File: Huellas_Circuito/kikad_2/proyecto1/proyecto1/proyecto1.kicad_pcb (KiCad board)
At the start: 2 copper layers, 54.5 x 77.5 mm, 6 parts, among them U1 ESP32-DEVKIT-V1

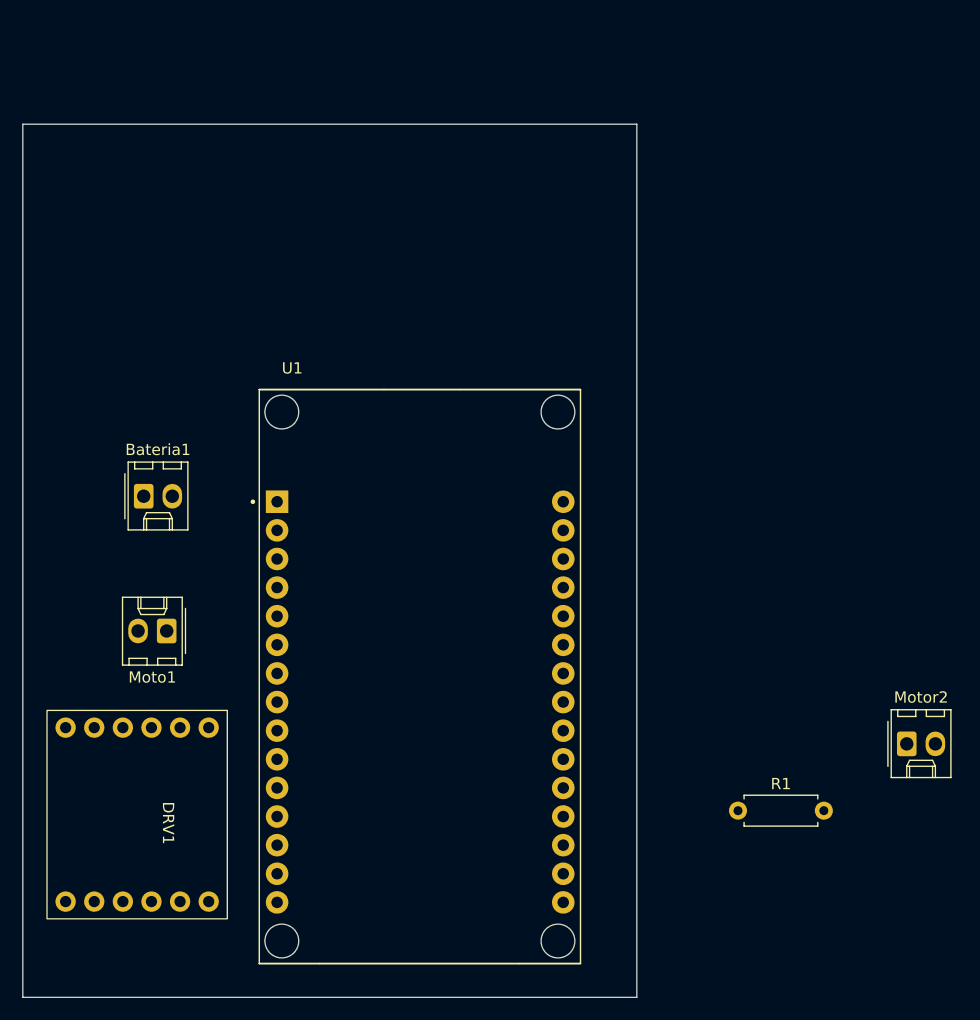
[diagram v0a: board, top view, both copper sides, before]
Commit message: Creacion_Footprint_Regul&Conectado
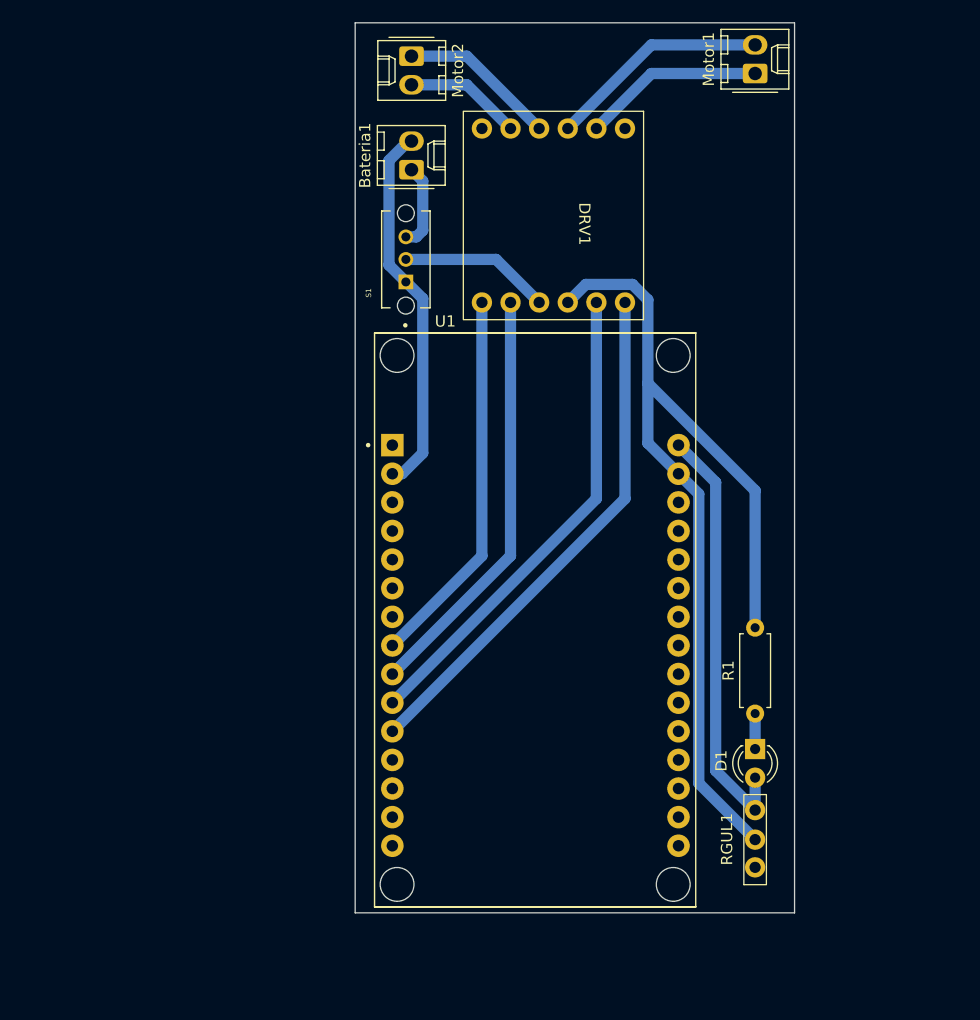
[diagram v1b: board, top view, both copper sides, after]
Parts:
- removed Moto1: Screw_Terminal_01x02, Connector_Molex:Molex_KK-254_AE-6410-02A_1x02_P2.54mm_Vertical
- added D1: LED, LED_THT:LED_D3.0mm, F.Cu at (145.5, 96.5)
- added Motor1: Screw_Terminal_01x02, Connector_Molex:Molex_KK-254_AE-6410-02A_1x02_P2.54mm_Vertical, F.Cu at (145.5, 36.5)
- added RGUL1: ~, Regulador:RGUL1, F.Cu at (145.5, 104.5)
- added S1: OS102011MS2QN1, OS102011MS2QN1:SW_OS102011MS2QN1, F.Cu at (114.5, 53.0)
- moved Motor2 75.2 mm to (115.0, 35.0), turned to -90 degrees
- moved DRV1 64.8 mm to (119.6, 39.9)
- moved Bateria1 37.5 mm to (115.0, 45.0), turned to 90 degrees
- moved U1 11.4 mm to (126.0, 85.0)
- moved R1 8.75 mm to (145.5, 93.3), turned to 90 degrees
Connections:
- U1 pad 30: /VIN -> /Vin
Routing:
- net GND: track 0.00 -> 119.3 mm
- net /PWM_MDER2: track 0.00 -> 46.6 mm
- net /PWM_MDER1: track 0.00 -> 43.0 mm
- net /Vin: track 0.00 -> 38.2 mm
- net /PWM_MIZQ2: track 0.00 -> 37.3 mm
- net /PWM_MIZQ1: track 0.00 -> 33.7 mm
- net /MIZQ2: track 0.00 -> 19.7 mm
- net /MIZQ1: track 0.00 -> 16.1 mm
- net /MDER1: track 0.00 -> 14.0 mm
- net /VDRV: track 0.00 -> 13.4 mm
- net /MDER2: track 0.00 -> 10.4 mm
- net Net-(Bateria1-Pin_1): track 0.00 -> 7.54 mm
- net Net-(D1-K): track 0.00 -> 3.15 mm
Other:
- board size 54.5 x 77.5 mm -> 39 x 79 mm

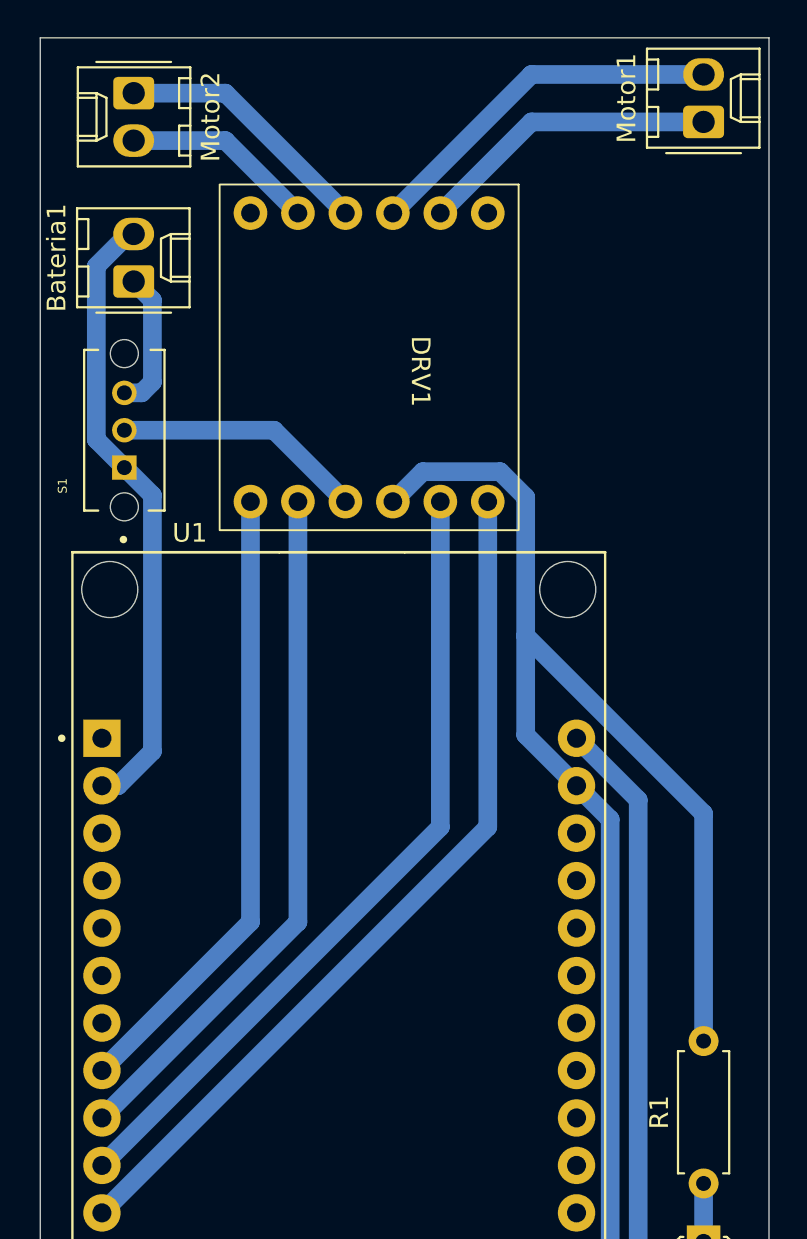
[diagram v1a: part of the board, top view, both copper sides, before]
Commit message: Actualizacion Huellas DRV (NotDefinitive)
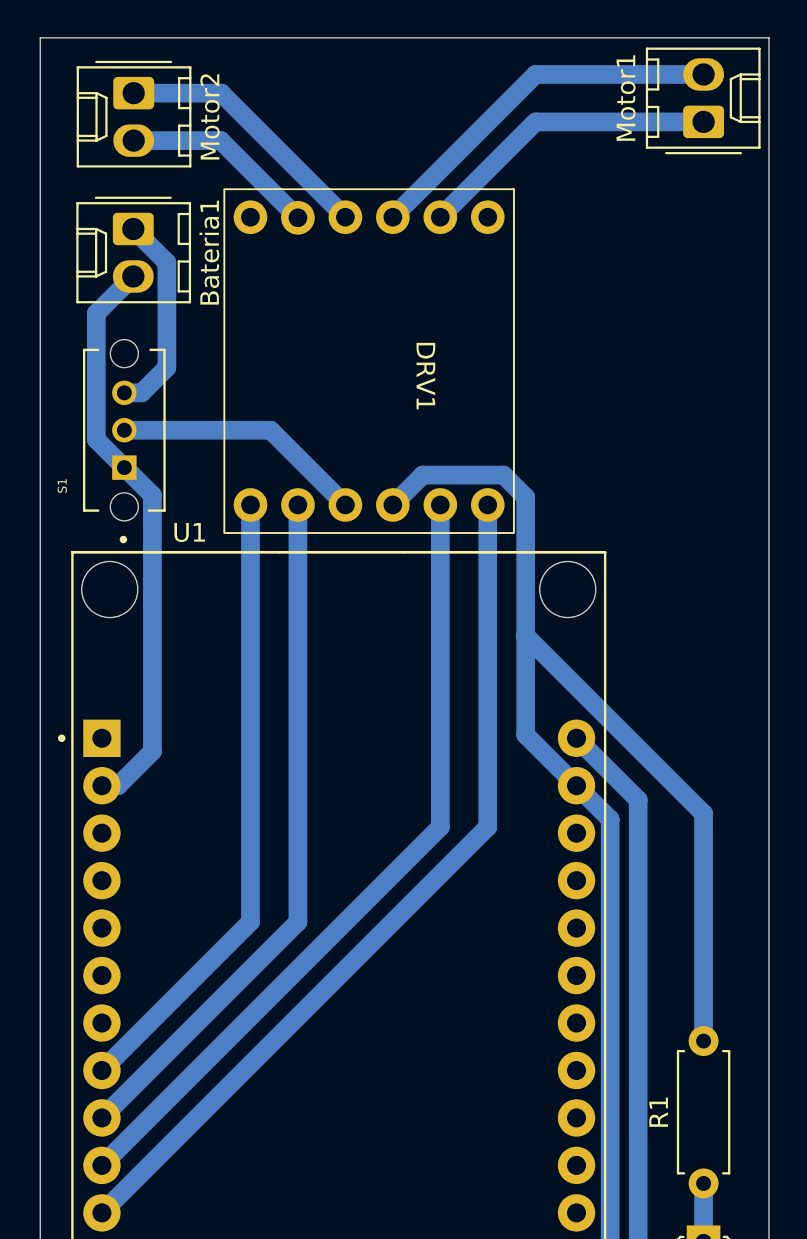
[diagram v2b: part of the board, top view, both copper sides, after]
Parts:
- moved Bateria1 2.81 mm to (115.0, 42.2), turned to -90 degrees
- moved DRV1 0.35 mm to (119.8, 40.1)
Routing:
- net Net-(Bateria1-Pin_1): track 7.54 -> 11.3 mm
- net GND: track 119.3 -> 116.7 mm

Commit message: Actualizacion Huellas DRV (NotDefinitive) V2
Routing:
- net /VDRV: track 13.5 -> 85.3 mm
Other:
- board size 39 x 79 mm -> 40 x 79 mm
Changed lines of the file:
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@@
 	(gr_rect
 		(start 110 32)
-		(end 149 111)
+		(end 150 111)
 		(stroke
 			(width 0.05)
@@
 		(end 122.33 53)
 		(width 1)
+		(layer "B.Cu")
+		(net 25)
+	)
+	(segment
+		(start 145.5 106.96)
+		(end 147.101 105.359)
+		(width 1)
+		(layer "B.Cu")
+		(net 25)
+	)
+	(segment
+		(start 147.101 105.359)
+		(end 147.101 66.008374)
+		(width 1)
+		(layer "B.Cu")
+		(net 25)
+	)
+	(segment
+		(start 147.101 66.008374)
+		(end 134.092626 53)
+		(width 1)
+		(layer "B.Cu")
+		(net 25)
+	)
+	(segment
+		(start 134.092626 53)
+		(end 122.33 53)
+		(width 1)

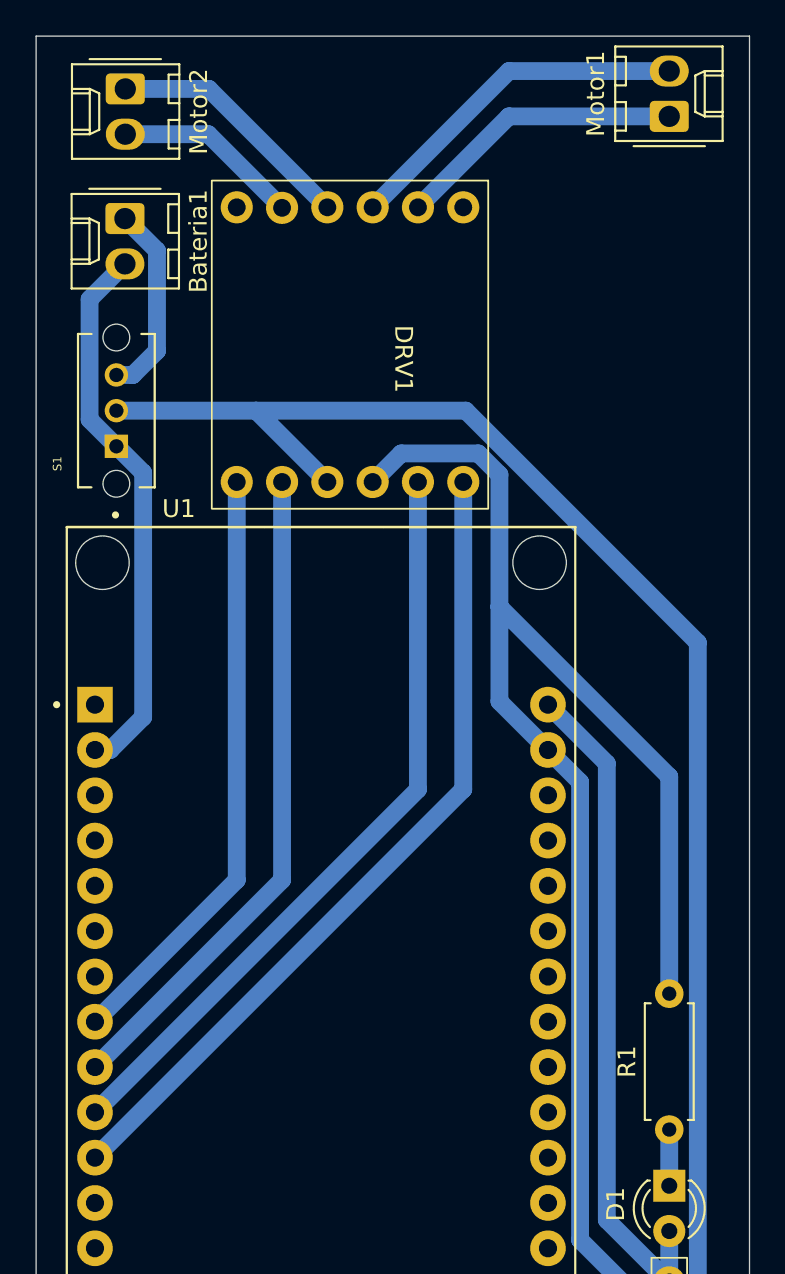
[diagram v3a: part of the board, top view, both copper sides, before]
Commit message: Actualizacion Huellas DRV (NotDefinitive) V2.2
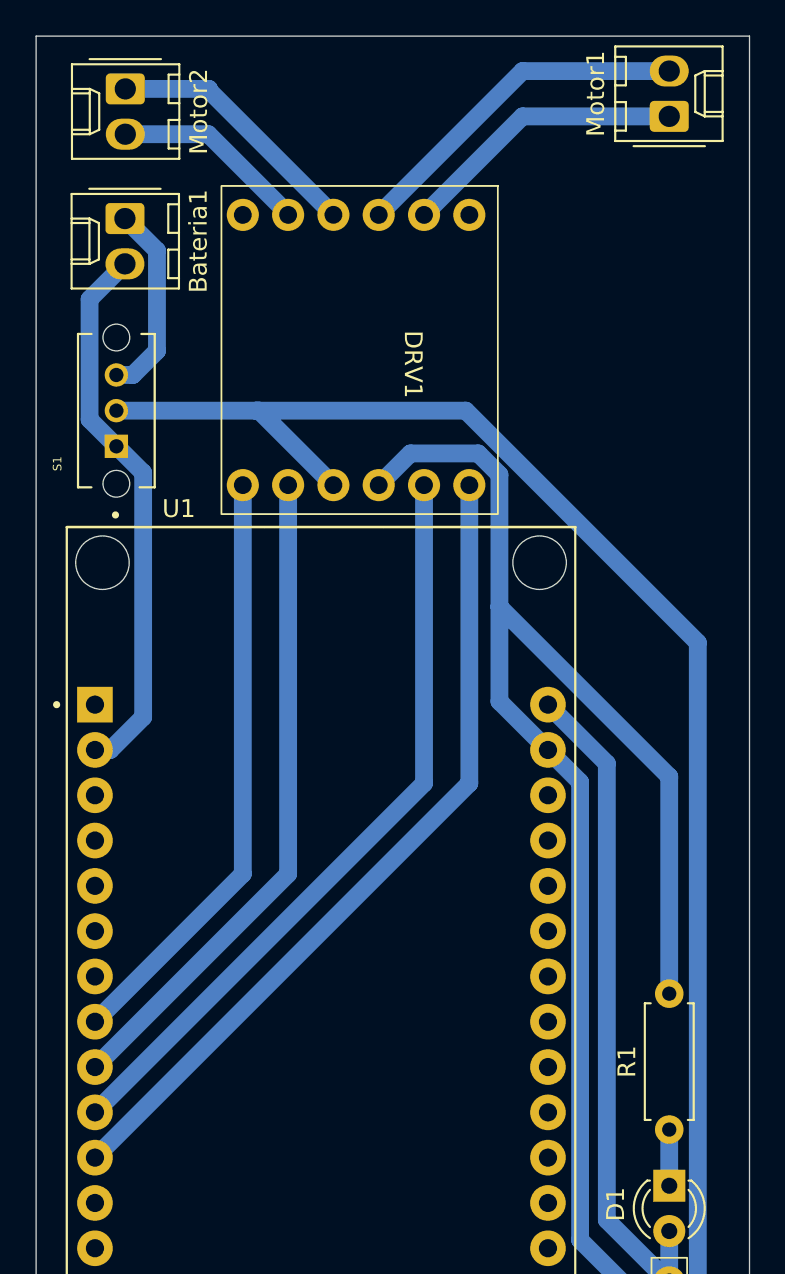
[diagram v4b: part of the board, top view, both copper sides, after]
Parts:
- moved DRV1 0.62 mm to (120.4, 40.4)
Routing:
- net /MDER1: track 14.1 -> 14.6 mm
- net /MDER2: track 10.5 -> 11.1 mm
